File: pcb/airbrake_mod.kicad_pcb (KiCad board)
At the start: 4 copper layers, 65.7 x 107.9 mm, 142 parts, among them J1 XT30PW-M, J2 Same Sky UJ20-C-H-G-SMT-P16-TR, J3 0436500415, J6 CNC_Tech_3220-14-0100-00, Q1 NTR4003N, Q2 NTR4003N, Q3 Si3407DV, Q4 NTR4003N, Q5 Si3407DV, Q6 NTR4003N, SW1 GSPTS0018, SW2 GSPTS0018, SW4 GSPTS0018, SW5 GSPTS0018, SW6 GSPTS0018, SW7 GSPTS0018, U1 STM32H730VBTx, U2 TPS561246DRLR, U3 ZXCT180A4W5, U4 USBLC6-2SC6, U5 W25Q128JVS, U6 LPS22DF, U7 LSM6DSV80X, U8 IIS2MDC, Y1 ECS-160-12-33B2Q-JES-TR3

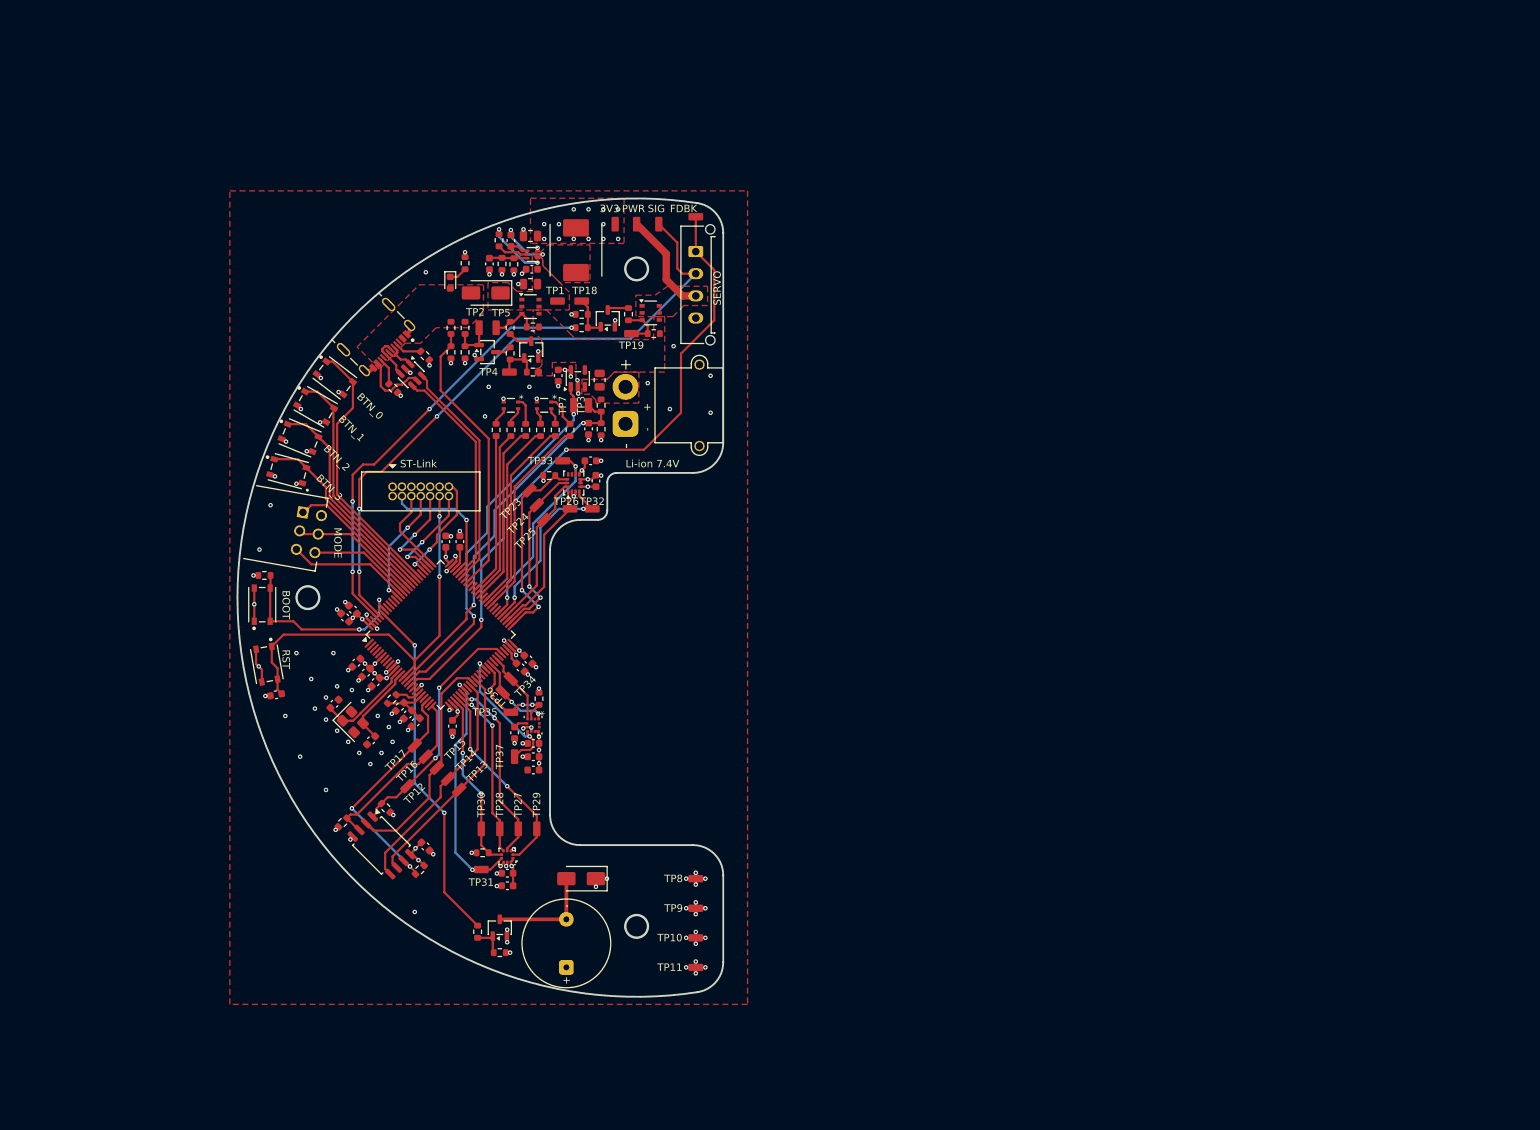
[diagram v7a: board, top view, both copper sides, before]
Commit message: Add back ground plane
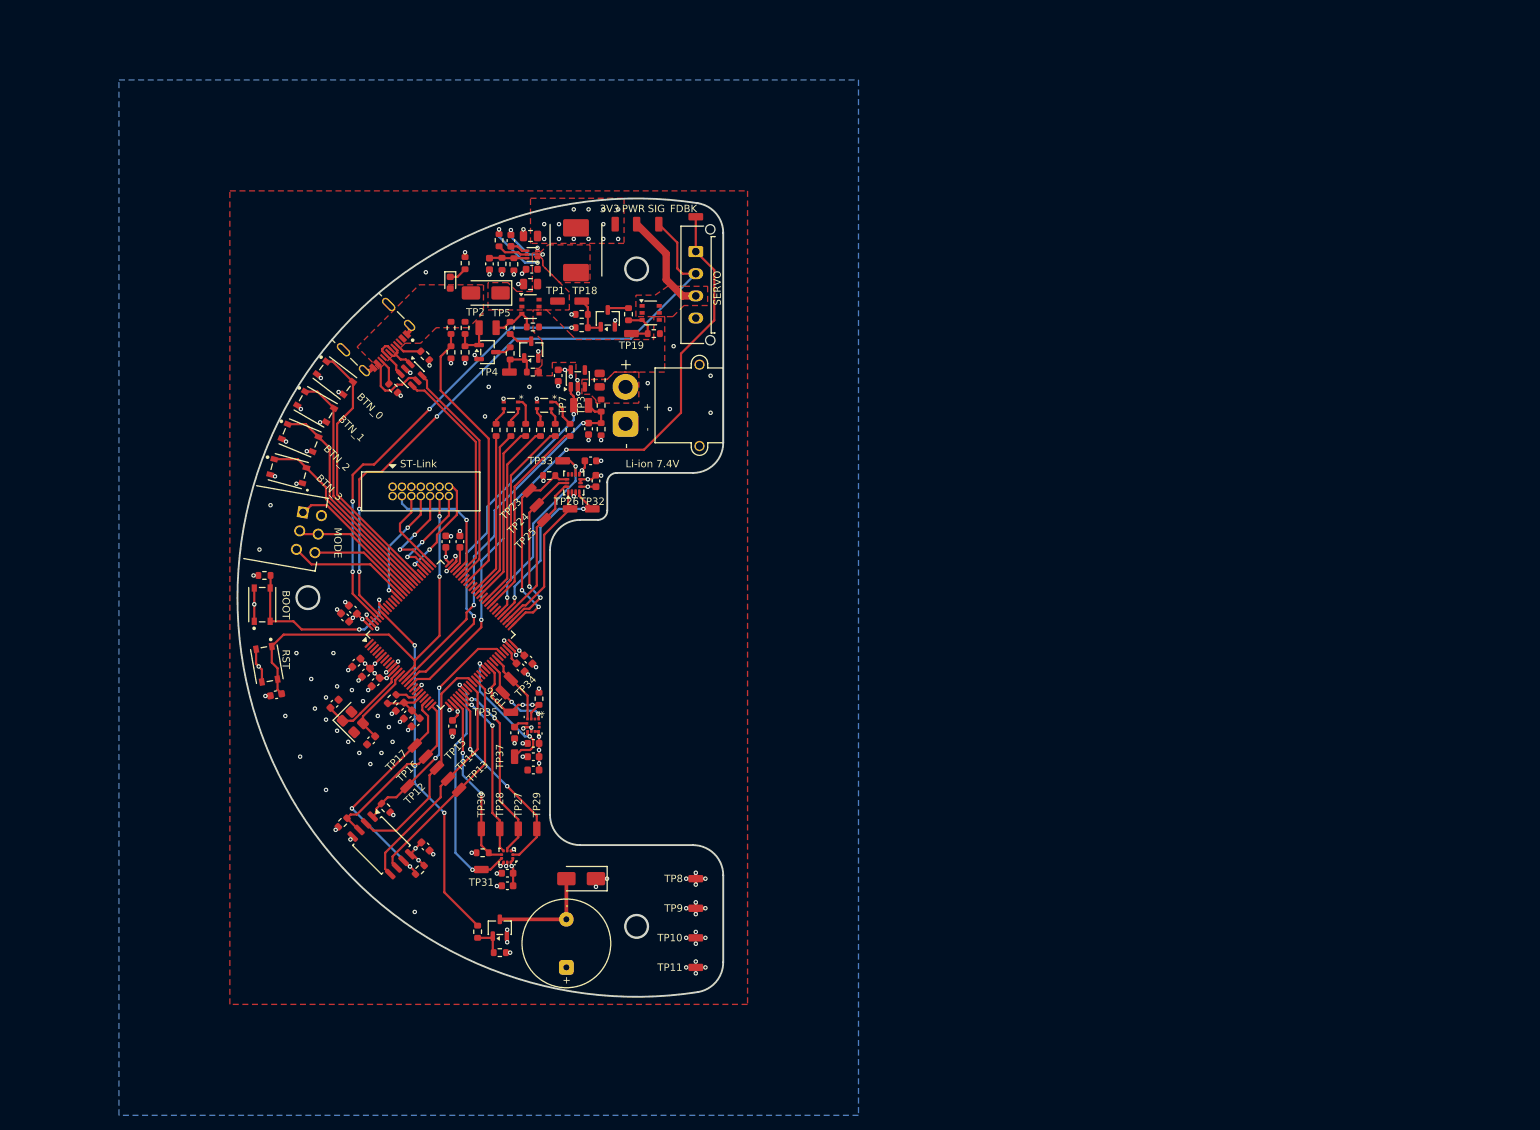
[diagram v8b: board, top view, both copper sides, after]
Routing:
- added copper zone on B.Cu, net GND
